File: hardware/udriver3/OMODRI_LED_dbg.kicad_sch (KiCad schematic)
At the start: 1 part

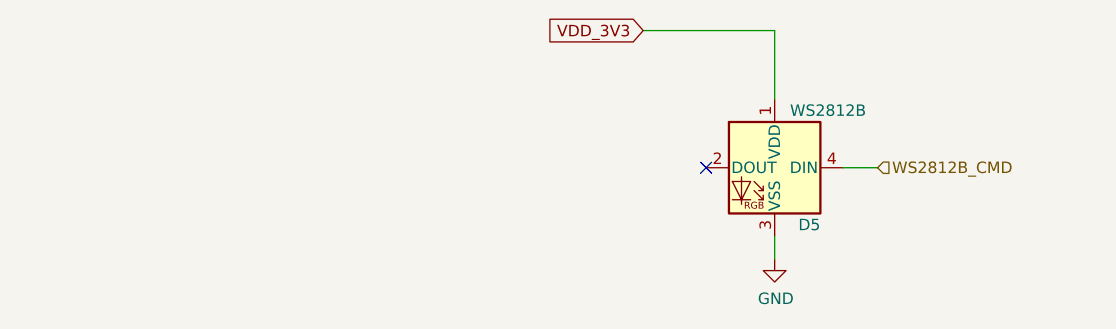
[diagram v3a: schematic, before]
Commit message: PCB updates - FSI protection added against FPC cable reverse connection - BOSCH BMI088 IMU added.
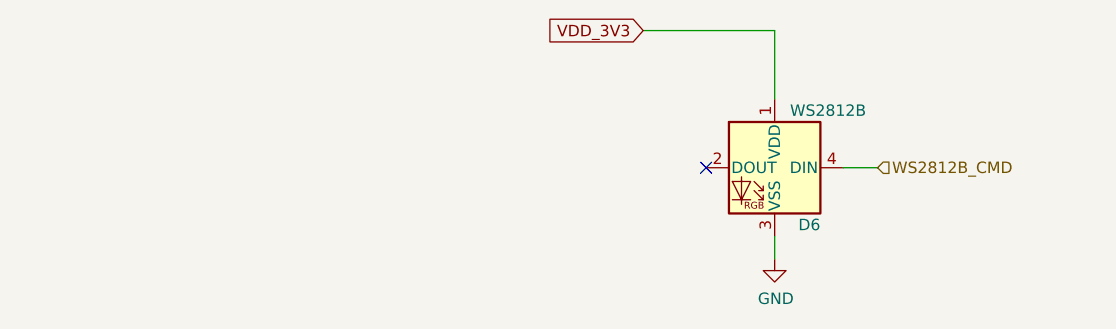
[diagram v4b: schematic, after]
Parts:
- renumbered D5 to D6
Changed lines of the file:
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@@
   (title_block
     (title "Open MOtor DRiver Initiative (OMODRI)")
-    (date "2022-10-05")
+    (date "2022-11-24")
     (rev "2.0")
     (company "LAAS/CNRS")
@@
   (symbol (lib_id "power:GND") (at 154.305 114.3 0) (unit 1)
     (in_bom yes) (on_board yes)
-    (property "Reference" "#PWR067" (id 0) (at 154.305 120.65 0)
+    (property "Reference" "#PWR068" (id 0) (at 154.305 120.65 0)
       (effects (font (size 1.27 1.27)) hide)
     )
@@
   (symbol (lib_id "LED:WS2812B") (at 154.305 104.14 0) (mirror y) (unit 1)
     (in_bom yes) (on_board yes)
-    (property "Reference" "D5" (id 0) (at 159.385 110.49 0)
+    (property "Reference" "D6" (id 0) (at 159.385 110.49 0)
       (effects (font (size 1.27 1.27)) (justify left))
     )

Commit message: PCB udpates. - add serial resistors on boot jumpers - modify config jumpers to be opened by default
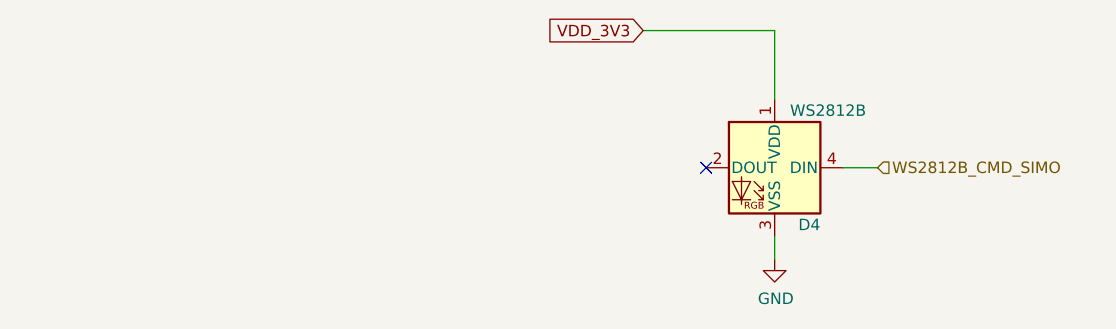
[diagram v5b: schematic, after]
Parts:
- renumbered D6 to D4
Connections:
- net WS2812B_CMD renamed WS2812B_CMD_SIMO
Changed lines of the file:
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@@
     )
   )
-  (hierarchical_label "WS2812B_CMD" (shape input) (at 165.735 104.14 0)
+  (hierarchical_label "WS2812B_CMD_SIMO" (shape input) (at 165.735 104.14 0)
     (effects (font (size 1.27 1.27)) (justify left))
   )
   (symbol (lib_id "power:GND") (at 154.305 114.3 0) (unit 1)
     (in_bom yes) (on_board yes)
-    (property "Reference" "#PWR068" (id 0) (at 154.305 120.65 0)
+    (property "Reference" "#PWR054" (id 0) (at 154.305 120.65 0)
       (effects (font (size 1.27 1.27)) hide)
     )
@@
   (symbol (lib_id "LED:WS2812B") (at 154.305 104.14 0) (mirror y) (unit 1)
     (in_bom yes) (on_board yes)
-    (property "Reference" "D6" (id 0) (at 159.385 110.49 0)
+    (property "Reference" "D4" (id 0) (at 159.385 110.49 0)
       (effects (font (size 1.27 1.27)) (justify left))
     )

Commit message: First release of uOmodri v3. Swap COM SPI. Modify CAN to CAN FD and bus sharing with RS485.
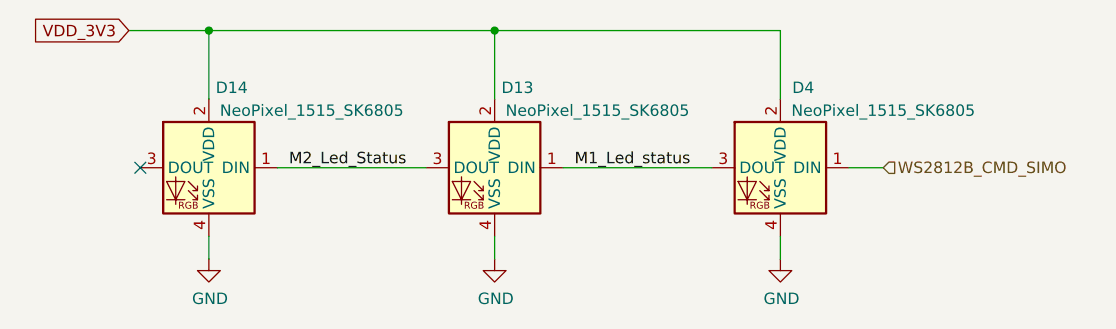
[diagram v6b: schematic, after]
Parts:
- removed D4: WS2812B, LED_SMD:LED_WS2812B_PLCC4_5.0x5.0mm_P3.2mm, symbol LED:WS2812B
- added D13, D14, D4: NeoPixel_1515_SK6805, udriver3:NeoPixel_SK6805_1.5x1.5mm, symbol omodri_lib:NeoPixel_1515_SK6805
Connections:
- net GND: now also D13.4 (VSS), D14.4 (VSS), D4.4 (VSS)
- net VDD_3V3: now also D13.2 (VDD), D14.2 (VDD), D4.2 (VDD)
- net WS2812B_CMD_SIMO: now also D4.1 (DIN)
- new net M1_Led_status: D13.1 (DIN), D4.3 (DOUT)
- new net M2_Led_Status: D13.3 (DOUT), D14.1 (DIN)

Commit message: Add JLCPCB components ref where it was matching.
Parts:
- D13, D14, D4: LCSC (none) -> C17701801
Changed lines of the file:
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@@
+      (effects (font (size 1.27 1.27)) hide)
+    )
+    (property "LCSC" "C17701801" (at 123.19 104.14 0)
       (effects (font (size 1.27 1.27)) hide)
     )
@@
       (effects (font (size 1.27 1.27)) hide)
     )
+    (property "LCSC" "C17701801" (at 154.94 104.14 0)
+      (effects (font (size 1.27 1.27)) hide)
+    )
     (pin "1")
     (pin "2")
@@
       (effects (font (size 1.27 1.27)) hide)
     )
+    (property "LCSC" "C17701801" (at 91.44 104.14 0)
+      (effects (font (size 1.27 1.27)) hide)
+    )
